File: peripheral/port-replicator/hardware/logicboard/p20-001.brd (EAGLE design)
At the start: 72 x 72 mm, 27 parts, among them IC11 74ALS04N, J0 DC9V, J11 AUDIO_JACK_3.5MM_PTH, J12 AUDIO_JACK_3.5MM_PTH, J13 AUDIO_JACK_3.5MM_PTH, J14 AUDIO_JACK_3.5MM_PTH, J7 DIN5, J8 DIN5, J9 DIN5, X0 MKDSN1,5/2-5,08

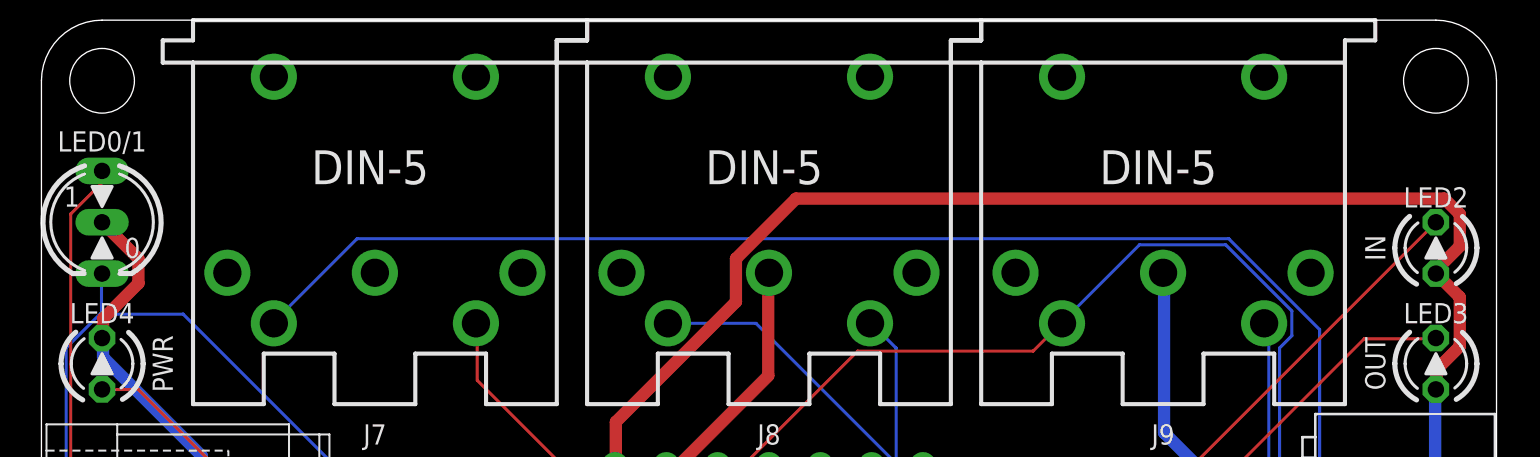
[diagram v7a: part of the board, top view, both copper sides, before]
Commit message: LED -> L.
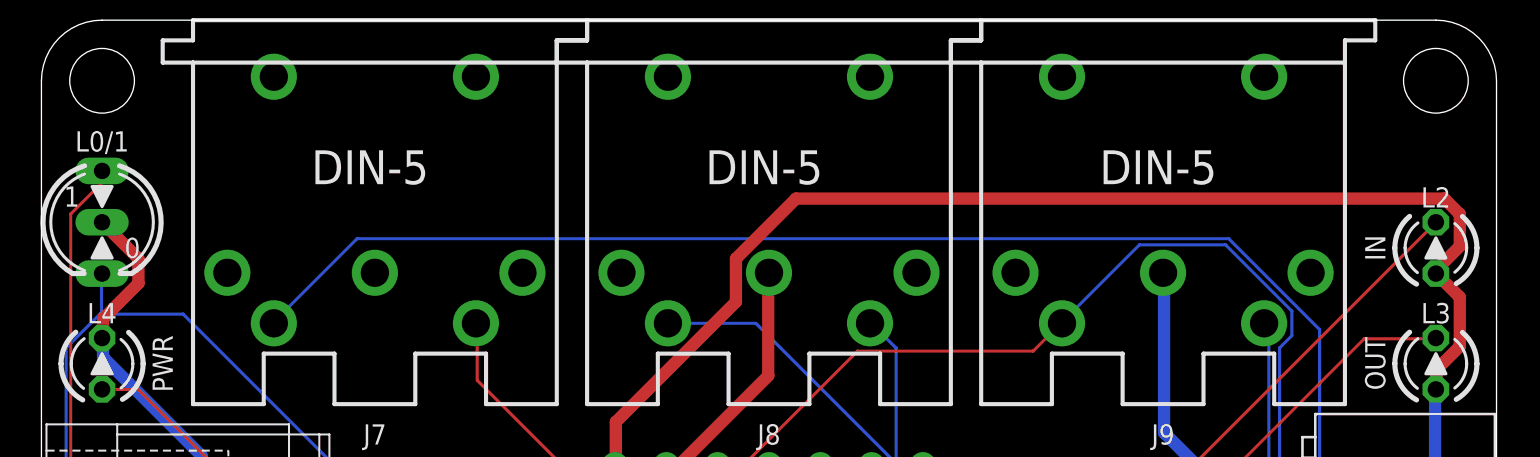
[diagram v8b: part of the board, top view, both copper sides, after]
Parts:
- renumbered LED0/1 to L0/1, LED2 to L2, LED3 to L3, LED4 to L4
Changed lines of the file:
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@@
 <attribute name="VALUE" x="46.8664" y="44.6886" size="0.9906" layer="27" ratio="10"/>
 </element>
-<element name="LED4" library="led" library_urn="urn:adsk.eagle:library:259" package="LED3MM" package3d_urn="urn:adsk.eagle:package:15797/1" value="PWR" x="3" y="55" smashed="yes" rot="R90">
+<element name="L4" library="led" library_urn="urn:adsk.eagle:library:259" package="LED3MM" package3d_urn="urn:adsk.eagle:package:15797/1" value="PWR" x="3" y="55" smashed="yes" rot="R90">
 <attribute name="NAME" x="3" y="57.5" size="1" layer="25" ratio="10" rot="R180" align="center"/>
 <attribute name="POPULARITY" value="97" x="3" y="55" size="1.778" layer="27" rot="R90" display="off"/>
 <attribute name="VALUE" x="4.651" y="56.905" size="1.27" layer="27" ratio="10" rot="R90"/>
 </element>
-<element name="LED2" library="led" library_urn="urn:adsk.eagle:library:259" package="LED3MM" package3d_urn="urn:adsk.eagle:package:15797/1" value="IN" x="69" y="60.73" smashed="yes" rot="R90">
+<element name="L2" library="led" library_urn="urn:adsk.eagle:library:259" package="LED3MM" package3d_urn="urn:adsk.eagle:package:15797/1" value="IN" x="69" y="60.73" smashed="yes" rot="R90">
 <attribute name="NAME" x="69" y="63.23" size="1" layer="25" ratio="10" rot="R180" align="center"/>
 <attribute name="POPULARITY" value="97" x="69" y="60.73" size="1.778" layer="27" rot="R90" display="off"/>
 <attribute name="VALUE" x="70.651" y="62.635" size="1.27" layer="27" ratio="10" rot="R90"/>
 </element>
-<element name="LED3" library="led" library_urn="urn:adsk.eagle:library:259" package="LED3MM" package3d_urn="urn:adsk.eagle:package:15797/1" value="OUT" x="69" y="55" smashed="yes" rot="R90">
+<element name="L3" library="led" library_urn="urn:adsk.eagle:library:259" package="LED3MM" package3d_urn="urn:adsk.eagle:package:15797/1" value="OUT" x="69" y="55" smashed="yes" rot="R90">
 <attribute name="NAME" x="69" y="57.5" size="1" layer="25" ratio="10" rot="R180" align="center"/>
 <attribute name="POPULARITY" value="97" x="69" y="55" size="1.778" layer="27" rot="R90" display="off"/>
@@
 <attribute name="VALUE" x="6.175" y="6.19" size="1.27" layer="27" rot="R90"/>
 </element>
-<element name="LED0/1" library="led" library_urn="urn:adsk.eagle:library:259" package="DUOLED-C-5MM" package3d_urn="urn:adsk.eagle:package:15851/1" value="" x="3" y="62" smashed="yes" rot="R270">
+<element name="L0/1" library="led" library_urn="urn:adsk.eagle:library:259" package="DUOLED-C-5MM" package3d_urn="urn:adsk.eagle:package:15851/1" value="" x="3" y="62" smashed="yes" rot="R270">
 <attribute name="NAME" x="3" y="66" size="1" layer="25" ratio="10" align="center"/>
 <attribute name="POPULARITY" value="1" x="3" y="62" size="1.778" layer="27" rot="R270" display="off"/>
@@
 <contactref element="IC11" pad="13"/>
 <contactref element="IC11" pad="5"/>
-<contactref element="LED4" pad="K"/>
+<contactref element="L4" pad="K"/>
 <contactref element="IC11" pad="7"/>
 <contactref element="X0" pad="1"/>
 <contactref element="S1" pad="1"/>
 <contactref element="S1" pad="2"/>
-<contactref element="LED0/1" pad="C"/>
+<contactref element="L0/1" pad="C"/>
 <contactref element="JP6" pad="2"/>
 <contactref element="SV2" pad="11"/>
@@
 <signal name="VCC" class="2">
 <contactref element="C11" pad="1"/>
-<contactref element="LED2" pad="A"/>
-<contactref element="LED3" pad="A"/>
+<contactref element="L2" pad="A"/>
+<contactref element="L3" pad="A"/>
 <contactref element="IC11" pad="14"/>
 <contactref element="SV2" pad="12"/>
@@
 </signal>
 <signal name="LEDMI">
-<contactref element="LED2" pad="K"/>
+<contactref element="L2" pad="K"/>
 <contactref element="R2" pad="2"/>
 <wire x1="54.0258" y1="47.0154" x2="51.5874" y2="47.0154" width="0.1524" layer="1"/>
@@
 </signal>
 <signal name="LEDMO">
-<contactref element="LED3" pad="K"/>
+<contactref element="L3" pad="K"/>
 <contactref element="R3" pad="2"/>
 <wire x1="53.2638" y1="44.0436" x2="51.5874" y2="44.0436" width="0.1524" layer="1"/>
@@
 <signal name="LEDPWR">
 <contactref element="R11" pad="1"/>
-<contactref element="LED4" pad="A"/>
+<contactref element="L4" pad="A"/>
 <wire x1="14.478" y1="44.0436" x2="20.4216" y2="44.0436" width="0.1524" layer="1"/>
 <wire x1="4.8006" y1="53.721" x2="14.478" y2="44.0436" width="0.1524" layer="1"/>
@@
 </signal>
 <signal name="LED0">
-<contactref element="LED0/1" pad="AR"/>
+<contactref element="L0/1" pad="AR"/>
 <contactref element="JP6" pad="1"/>
 <contactref element="SV2" pad="19"/>
@@
 </signal>
 <signal name="LED1">
-<contactref element="LED0/1" pad="AX"/>
+<contactref element="L0/1" pad="AX"/>
 <contactref element="JP6" pad="3"/>
 <wire x1="2.9718" y1="63.9318" x2="2.9718" y2="64.4652" width="0.1524" layer="1"/>
